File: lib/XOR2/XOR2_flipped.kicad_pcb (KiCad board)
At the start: 2 copper layers, 10 parts, among them P1 PMOS, P2 PMOS, P3 PMOS, P4 PMOS, P5 PMOS

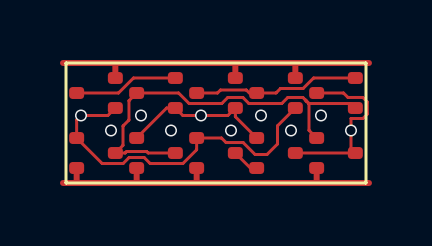
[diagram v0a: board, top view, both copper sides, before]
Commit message: Layout of XOR2 and XNOR2, in both orientations. That nut was hard to crack !!
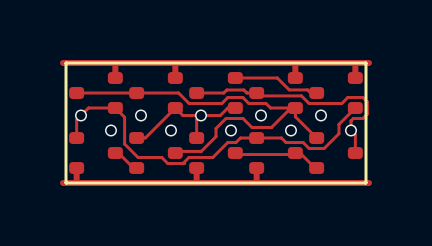
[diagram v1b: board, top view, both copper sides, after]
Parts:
- moved N3 4.47 mm to (9.00, 1.00), turned to 180 degrees
- moved N4 2.83 mm to (5.00, 1.00), turned to 180 degrees
- moved N5 2.83 mm to (7.00, 1.00), turned to 180 degrees
- moved N1 2.00 mm to (1.00, 1.00), turned to 180 degrees
- moved N2 2.00 mm to (3.00, 1.00), turned to 180 degrees
- moved P1 2.00 mm to (1.00, 3.00), turned to 0 degrees
- moved P2 2.00 mm to (3.00, 3.00), turned to 0 degrees
- moved P3 2.00 mm to (7.00, 3.00), turned to 0 degrees
- moved P4 2.00 mm to (5.00, 3.00), turned to 0 degrees
- moved P5 2.00 mm to (9.00, 3.00), turned to 0 degrees
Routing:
- net pmid: track 5.58 -> 2.96 mm
- net sndPA: track 3.50 -> 0.92 mm
- net Y: track 6.03 -> 8.24 mm
- net sndNA: track 0.92 -> 2.72 mm
- net A: track 11.7 -> 12.7 mm
